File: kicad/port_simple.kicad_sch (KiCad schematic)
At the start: 17 parts, among them J801 USB3_A, SW801 SW_Push, U901 AP22804AW5

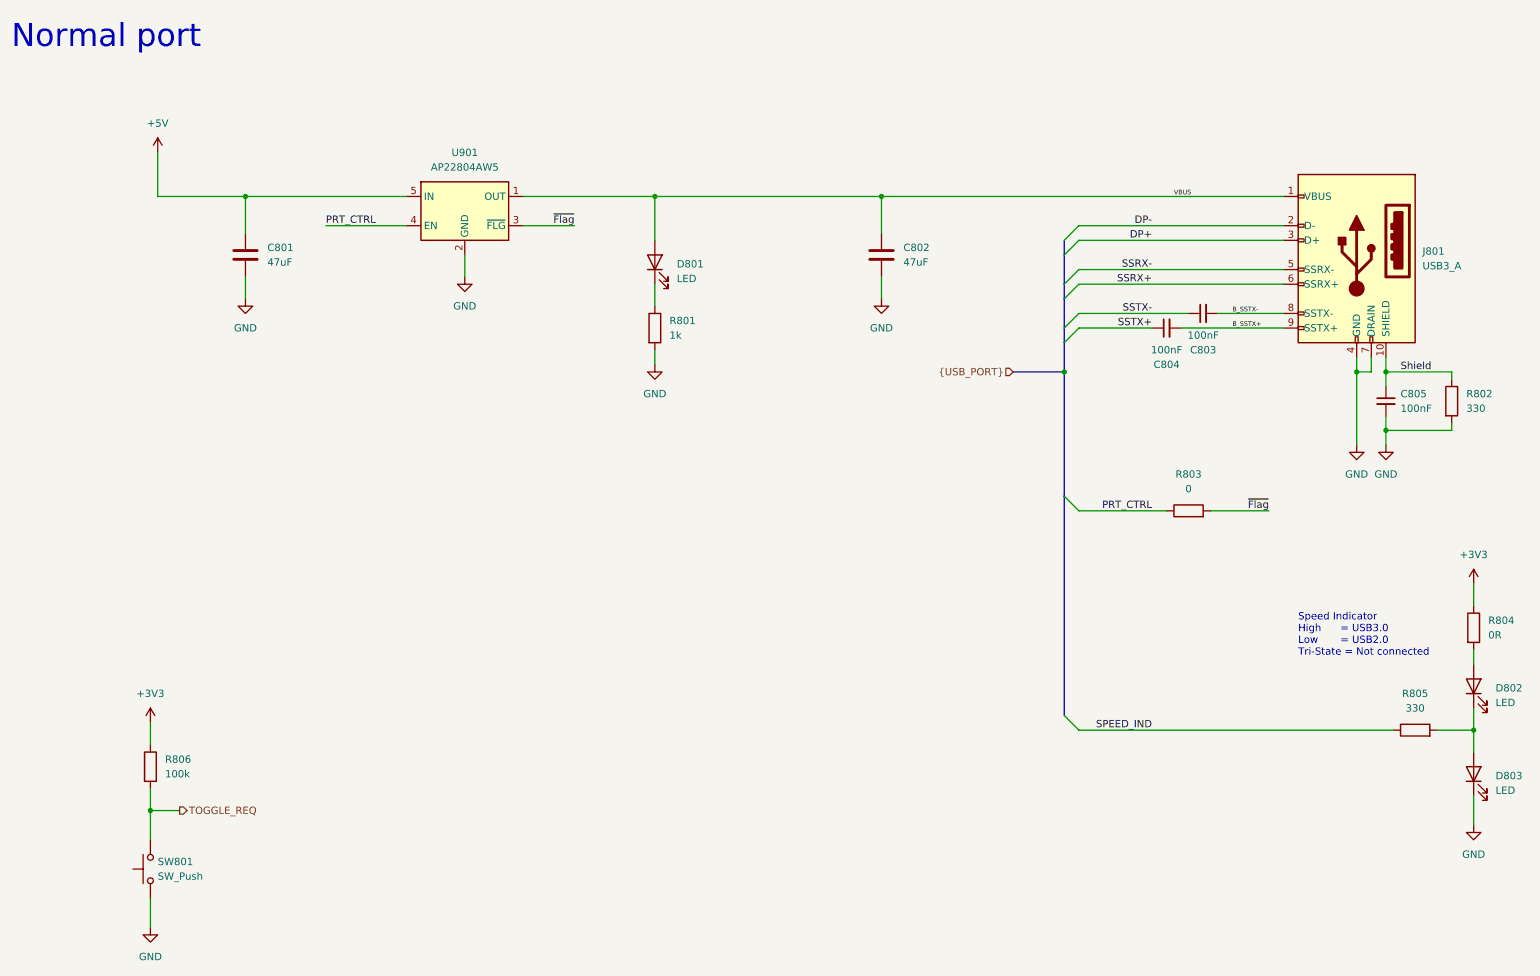
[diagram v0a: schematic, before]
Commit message: First rough placement
Just to get an idea on how it might look like
Added trace widts for Differential pairs
Using 6 layers, because it makes power management easier.
Rather large PCB, but better to big, then to small.
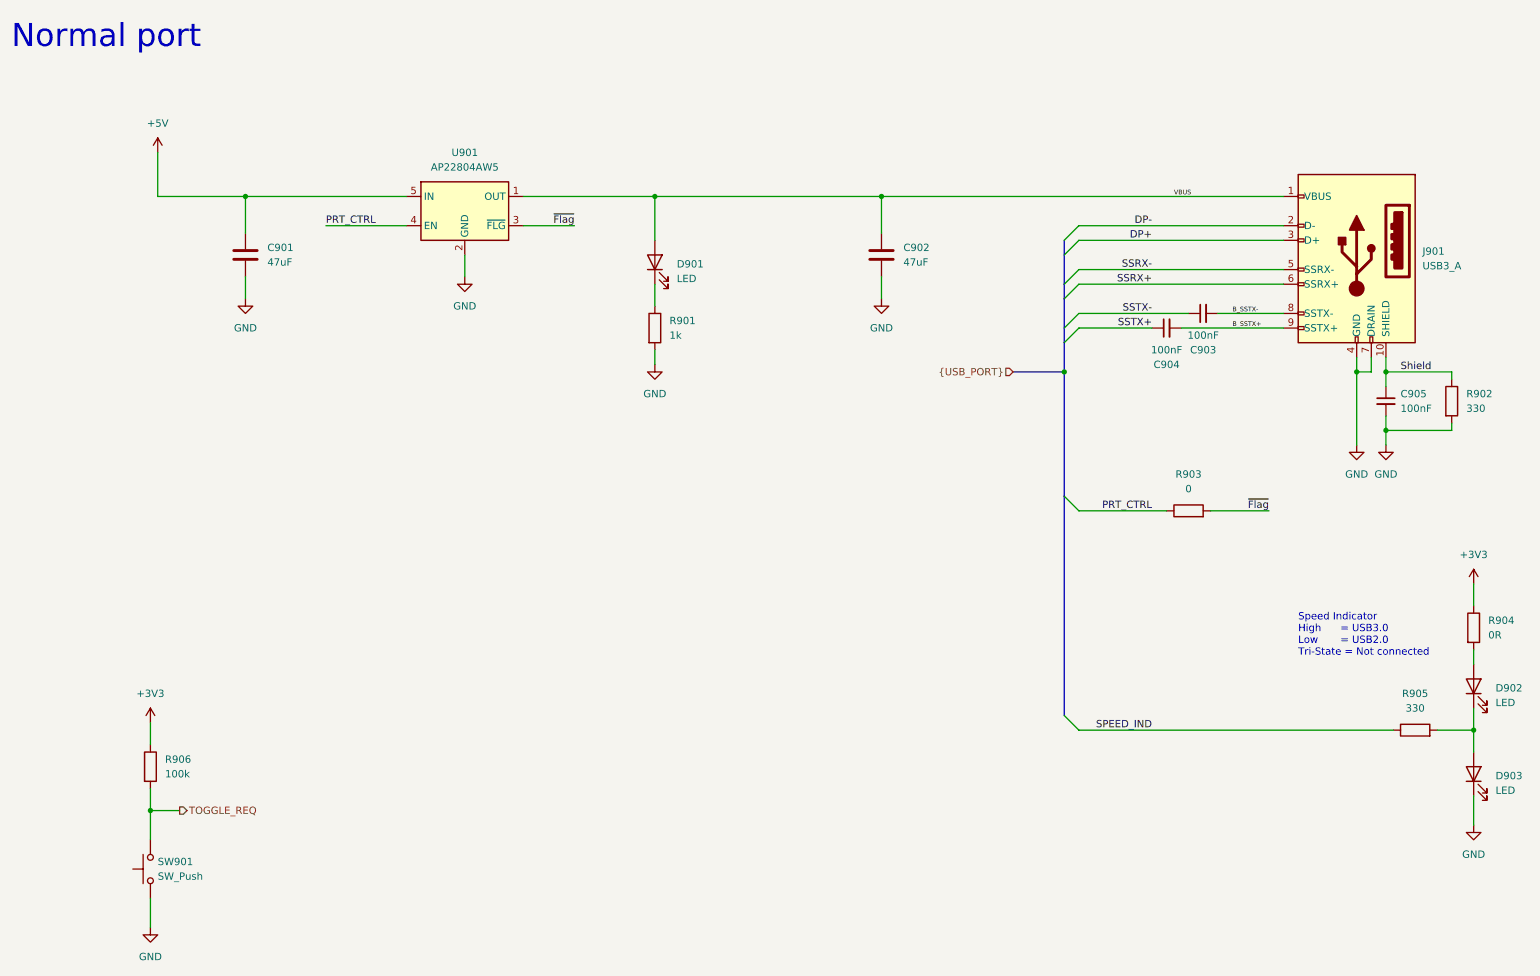
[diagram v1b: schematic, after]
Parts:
- C901: renamed from C801; footprint Capacitor_SMD:C_0805_2012Metric -> Capacitor_SMD:C_1210_3225Metric
- C902: renamed from C802; footprint Capacitor_SMD:C_0805_2012Metric -> Capacitor_SMD:C_1210_3225Metric
- renumbered C803 to C903, C804 to C904, C805 to C905, D801 to D901, D802 to D902, D803 to D903, J801 to J901, R801 to R901, R802 to R902, R803 to R903, R804 to R904, R805 to R905, R806 to R906, SW801 to SW901
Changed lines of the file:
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@@
 		(dnp no)
 		(fields_autoplaced yes)
-		(property "Reference" "#PWR0801"
+		(property "Reference" "#PWR0901"
 			(at 39.37 40.64 0)
 			(effects
@@
 		(dnp no)
 		(fields_autoplaced yes)
-		(property "Reference" "C805"
+		(property "Reference" "C905"
 			(at 255.27 78.7462 0)
 			(effects
@@
 		(dnp no)
 		(fields_autoplaced yes)
-		(property "Reference" "R805"
+		(property "Reference" "R905"
 			(at 257.81 130.81 90)
 			(effects
@@
 		(dnp no)
 		(fields_autoplaced yes)
-		(property "Reference" "R803"
+		(property "Reference" "R903"
 			(at 218.44 92.71 90)
 			(effects
@@
 		(dnp no)
 		(fields_autoplaced yes)
-		(property "Reference" "#PWR0808"
+		(property "Reference" "#PWR0908"
 			(at 267.97 115.57 0)
 			(effects
@@
 		(dnp no)
 		(fields_autoplaced yes)
-		(property "Reference" "D801"
+		(property "Reference" "D901"
 			(at 129.54 56.1974 90)
 			(effects
@@
 		(dnp no)
 		(fields_autoplaced yes)
-		(property "Reference" "SW801"
+		(property "Reference" "SW901"
 			(at 39.37 160.0199 90)
 			(effects
@@
 		(dnp no)
 		(fields_autoplaced yes)
-		(property "Reference" "J801"
+		(property "Reference" "J901"
 			(at 259.08 53.9749 0)
 			(effects
@@
 		(dnp no)
 		(fields_autoplaced yes)
-		(property "Reference" "#PWR0811"
+		(property "Reference" "#PWR0911"
 			(at 38.1 177.8 0)
 			(effects
@@
 		(dnp no)
 		(fields_autoplaced yes)
-		(property "Reference" "R806"
+		(property "Reference" "R906"
 			(at 40.64 142.2399 0)
 			(effects
@@
 		(dnp no)
 		(fields_autoplaced yes)
-		(property "Reference" "#PWR0810"
+		(property "Reference" "#PWR0910"
 			(at 267.97 160.02 0)
 			(effects
@@
 		(dnp no)
 		(fields_autoplaced yes)
-		(property "Reference" "D803"
+		(property "Reference" "D903"
 			(at 271.78 145.0974 90)
 			(effects
@@
 		(dnp no)
 		(fields_autoplaced yes)
-		(property "Reference" "R802"
+		(property "Reference" "R902"
 			(at 266.7 78.7399 0)
 			(effects
@@
 		(on_board yes)
 		(dnp no)
-		(property "Reference" "C804"
+		(property "Reference" "C904"
 			(at 214.6363 73.66 90)
 			(effects
@@
 		(dnp no)
 		(fields_autoplaced yes)
-		(property "Reference" "C801"
+		(property "Reference" "C901"
 			(at 58.42 53.3399 0)
 			(effects
@@
 			)
 		)
-		(property "Footprint" "Capacitor_SMD:C_0805_2012Metric"
+		(property "Footprint" "Capacitor_SMD:C_1210_3225Metric"
 			(at 55.5752 58.42 0)
 			(effects
@@
 		(dnp no)
 		(fields_autoplaced yes)
-		(property "Reference" "#PWR0804"
+		(property "Reference" "#PWR0904"
 			(at 165.1 68.58 0)
 			(effects
@@
 		(dnp no)
 		(fields_autoplaced yes)
-		(property "Reference" "#PWR0803"
+		(property "Reference" "#PWR0903"
 			(at 54.61 68.58 0)
 			(effects
@@
 		(dnp no)
 		(fields_autoplaced yes)
-		(property "Reference" "C802"
+		(property "Reference" "C902"
 			(at 168.91 53.3399 0)
 			(effects
@@
 			)
 		)
-		(property "Footprint" "Capacitor_SMD:C_0805_2012Metric"
+		(property "Footprint" "Capacitor_SMD:C_1210_3225Metric"
 			(at 166.0652 58.42 0)
 			(effects
@@
 		(dnp no)
 		(fields_autoplaced yes)
-		(property "Reference" "R804"
+		(property "Reference" "R904"
 			(at 270.51 118.1099 0)
 			(effects
@@
 		(dnp no)
 		(fields_autoplaced yes)
-		(property "Reference" "#PWR0809"
+		(property "Reference" "#PWR0909"
 			(at 38.1 139.7 0)
 			(effects
@@
 		(dnp no)
 		(fields_autoplaced yes)
-		(property "Reference" "#PWR0805"
+		(property "Reference" "#PWR0905"
 			(at 125.73 80.01 0)
 			(effects
@@
 		(on_board yes)
 		(dnp no)
-		(property "Reference" "C803"
+		(property "Reference" "C903"
 			(at 220.9863 71.12 90)
 			(effects
@@
 		(dnp no)
 		(fields_autoplaced yes)
-		(property "Reference" "R801"
+		(property "Reference" "R901"
 			(at 128.27 66.0399 0)
 			(effects
@@
 		(dnp no)
 		(fields_autoplaced yes)
-		(property "Reference" "D802"
+		(property "Reference" "D902"
 			(at 271.78 129.8574 90)
 			(effects

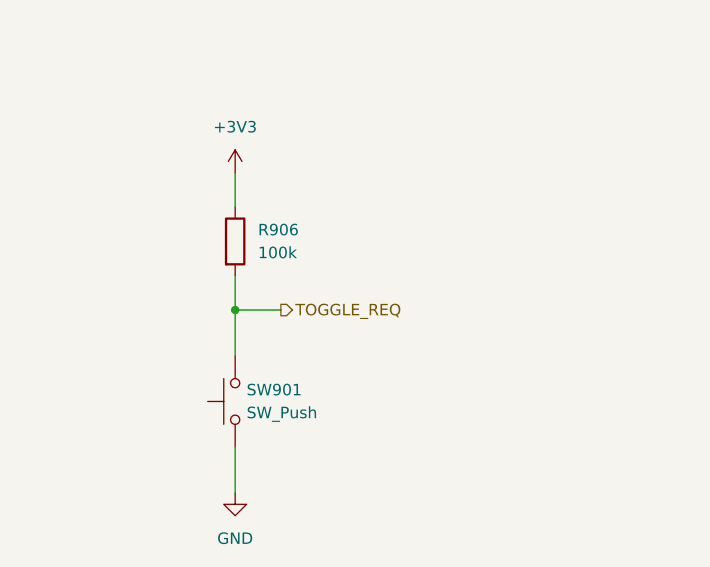
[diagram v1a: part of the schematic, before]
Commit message: Replace 1.2V LDO with switching regulator
It just feels more reliable.
Also added 0R resistors between switch and alert signal. My hope is
that I can tell the switch to diable the port by pulling the
overcurrent low.
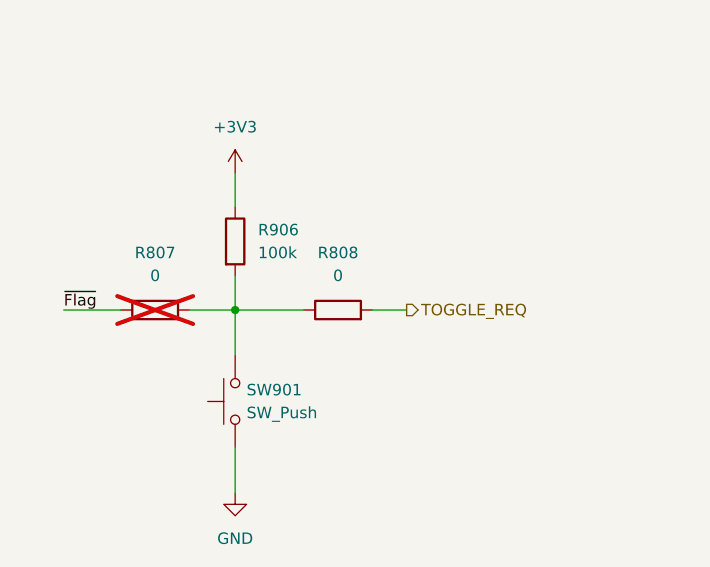
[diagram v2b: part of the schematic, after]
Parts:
- added R807, R808: 0, Resistor_SMD:R_0603_1608Metric, symbol Device:R
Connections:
- net TOGGLE_REQ: now also R808.2; no longer R906.2, SW901.2
- net ~{Flag}: now also R807.1
- new net: R807.2, R808.1, R906.2, SW901.2
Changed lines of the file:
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@@
+	(wire
+		(pts
+			(xy 19.05 151.13) (xy 25.4 151.13)
+		)
+		(stroke
+			(width 0)
+			(type default)
+		)
+	)
 	(wire
 		(pts
@@
 		)
 	)
+	(wire
+		(pts
+			(xy 53.34 151.13) (xy 57.15 151.13)
+		)
+		(stroke
+			(width 0)
+			(type default)
+		)
+	)
 	(bus
 		(pts
@@
 	(wire
 		(pts
-			(xy 38.1 151.13) (xy 43.18 151.13)
+			(xy 38.1 151.13) (xy 45.72 151.13)
 		)
 		(stroke
@@
 		(pts
 			(xy 102.87 49.53) (xy 111.76 49.53)
+		)
+		(stroke
+			(width 0)
+			(type default)
+		)
+	)
+	(wire
+		(pts
+			(xy 33.02 151.13) (xy 38.1 151.13)
 		)
 		(stroke
@@
 		)
 	)
-	(label "SSRX-"
-		(at 212.09 57.15 180)
+	(label "~{Flag}"
+		(at 19.05 151.13 0)
 		(fields_autoplaced yes)
 		(effects
@@
 				(size 1.27 1.27)
 			)
-			(justify right bottom)
-		)
-	)
-	(label "Shield"
-		(at 255.27 74.93 0)
+			(justify left bottom)
+		)
+	)
+	(label "SSRX-"
+		(at 212.09 57.15 180)
 		(fields_autoplaced yes)
 		(effects
@@
 				(size 1.27 1.27)
 			)
-			(justify left bottom)
-		)
-	)
-	(label "SSTX+"
-		(at 212.09 67.31 180)
+			(justify right bottom)
+		)
+	)
+	(label "Shield"
+		(at 255.27 74.93 0)
 		(fields_autoplaced yes)
 		(effects
@@
 				(size 1.27 1.27)
 			)
-			(justify right bottom)
-		)
-	)
-	(label "DP+"
-		(at 212.09 52.07 180)
+			(justify left bottom)
+		)
+	)
+	(label "SSTX+"
+		(at 212.09 67.31 180)
 		(fields_autoplaced yes)
 		(effects
@@
 		)
 	)
+	(label "DP+"
+		(at 212.09 52.07 180)
+		(fields_autoplaced yes)
+		(effects
+			(font
+				(size 1.27 1.27)
+			)
+			(justify right bottom)
+		)
+	)
 	(label "B_SSTX-"
 		(at 226.06 64.77 0)
@@
 	(hierarchical_label "TOGGLE_REQ"
 		(shape output)
-		(at 43.18 151.13 0)
+		(at 57.15 151.13 0)
 		(fields_autoplaced yes)
 		(effects
@@
 				(path "/fa2d0b8b-d66f-4d1f-bda6-9ad6b6242db5/cfed4b24-84a1-4de4-9f0d-ad8bcfe8d876"
 					(reference "C1005")
+					(unit 1)
+				)
+			)
+		)
+	)
+	(symbol
+		(lib_id "Device:R")
+		(at 49.53 151.13 90)
+		(unit 1)
+		(exclude_from_sim no)
+		(in_bom yes)
+		(on_board yes)
+		(dnp no)
+		(fields_autoplaced yes)
+		(property "Reference" "R808"
+			(at 49.53 144.78 90)
+			(effects
+				(font
+					(size 1.27 1.27)
+				)
+			)
+		)
+		(property "Value" "0"
+			(at 49.53 147.32 90)
+			(effects
+				(font
+					(size 1.27 1.27)
+				)
+			)
+		)
+		(property "Footprint" "Resistor_SMD:R_0603_1608Metric"
+			(at 49.53 152.908 90)
+			(effects
+				(font
+					(size 1.27 1.27)
+				)
+				(hide yes)
+			)
+		)
+		(property "Datasheet" "~"
+			(at 49.53 151.13 0)
+			(effects
+				(font
+					(size 1.27 1.27)
+				)
+				(hide yes)
+			)
+		)
+		(property "Description" "Resistor"
+			(at 49.53 151.13 0)
+			(effects
+				(font
+					(size 1.27 1.27)
+				)
+				(hide yes)
+			)
+		)
+		(pin "1"
+		)
+		(pin "2"
+		)
+		(instances
+			(project "usb3-hub"
+				(path "/fa2d0b8b-d66f-4d1f-bda6-9ad6b6242db5/8630f389-c276-479d-b9fc-6296f8ff2e6c"
+					(reference "R908")
+					(unit 1)
+				)
+				(path "/fa2d0b8b-d66f-4d1f-bda6-9ad6b6242db5/9f8a5db8-b0b8-4650-a3b6-687f7418ce2a"
+					(reference "R808")
+					(unit 1)
+				)
+				(path "/fa2d0b8b-d66f-4d1f-bda6-9ad6b6242db5/cfed4b24-84a1-4de4-9f0d-ad8bcfe8d876"
+					(reference "R1008")
 					(unit 1)
 				)
@@
 					(unit 1)
 				)
+			)
+		)
+	)
+	(symbol
+		(lib_id "Device:R")
+		(at 29.21 151.13 90)
+		(unit 1)
+		(exclude_from_sim no)
+		(in_bom yes)
+		(on_board yes)
+		(dnp yes)
+		(fields_autoplaced yes)
+		(property "Reference" "R807"
+			(at 29.21 144.78 90)
+			(effects
+				(font
+					(size 1.27 1.27)
+				)
+			)
+		)
+		(property "Value" "0"
+			(at 29.21 147.32 90)
+			(effects
+				(font
+					(size 1.27 1.27)
+				)
+			)
+		)
+		(property "Footprint" "Resistor_SMD:R_0603_1608Metric"
+			(at 29.21 152.908 90)
+			(effects
+				(font
+					(size 1.27 1.27)
+				)
+				(hide yes)
+			)
+		)
+		(property "Datasheet" "~"
+			(at 29.21 151.13 0)
+			(effects
+				(font
+					(size 1.27 1.27)
+				)
+				(hide yes)
+			)
+		)
+		(property "Description" "Resistor"
+			(at 29.21 151.13 0)
+			(effects
+				(font
+					(size 1.27 1.27)
+				)
+				(hide yes)
+			)
+		)
+		(pin "1"
+		)
+		(pin "2"
+		)
+		(instances
+			(project "usb3-hub"
+				(path "/fa2d0b8b-d66f-4d1f-bda6-9ad6b6242db5/8630f389-c276-479d-b9fc-6296f8ff2e6c"
+					(reference "R907")
+					(unit 1)
+				)
+				(path "/fa2d0b8b-d66f-4d1f-bda6-9ad6b6242db5/9f8a5db8-b0b8-4650-a3b6-687f7418ce2a"
+					(reference "R807")
+					(unit 1)
+				)
+				(path "/fa2d0b8b-d66f-4d1f-bda6-9ad6b6242db5/cfed4b24-84a1-4de4-9f0d-ad8bcfe8d876"
+					(reference "R1007")
+					(unit 1)
+				)

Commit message: Some more routing
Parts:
- renumbered R807 to R907, R808 to R908
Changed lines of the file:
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@@
 		(dnp no)
 		(fields_autoplaced yes)
-		(property "Reference" "R808"
+		(property "Reference" "R908"
 			(at 49.53 144.78 90)
 			(effects
@@
 		(dnp yes)
 		(fields_autoplaced yes)
-		(property "Reference" "R807"
+		(property "Reference" "R907"
 			(at 29.21 144.78 90)
 			(effects
